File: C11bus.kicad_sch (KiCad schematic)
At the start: 44 parts, among them IC2 THVD1450DRBR, IC4 THVD1450DRBR, IC5 THVD1450DRBR, J21 Conn_01x16, J22 RTBUS.out, J23 RTBUS.in, U3 74AHC1G02, U4 74AHC1G02, U7 INA181A4

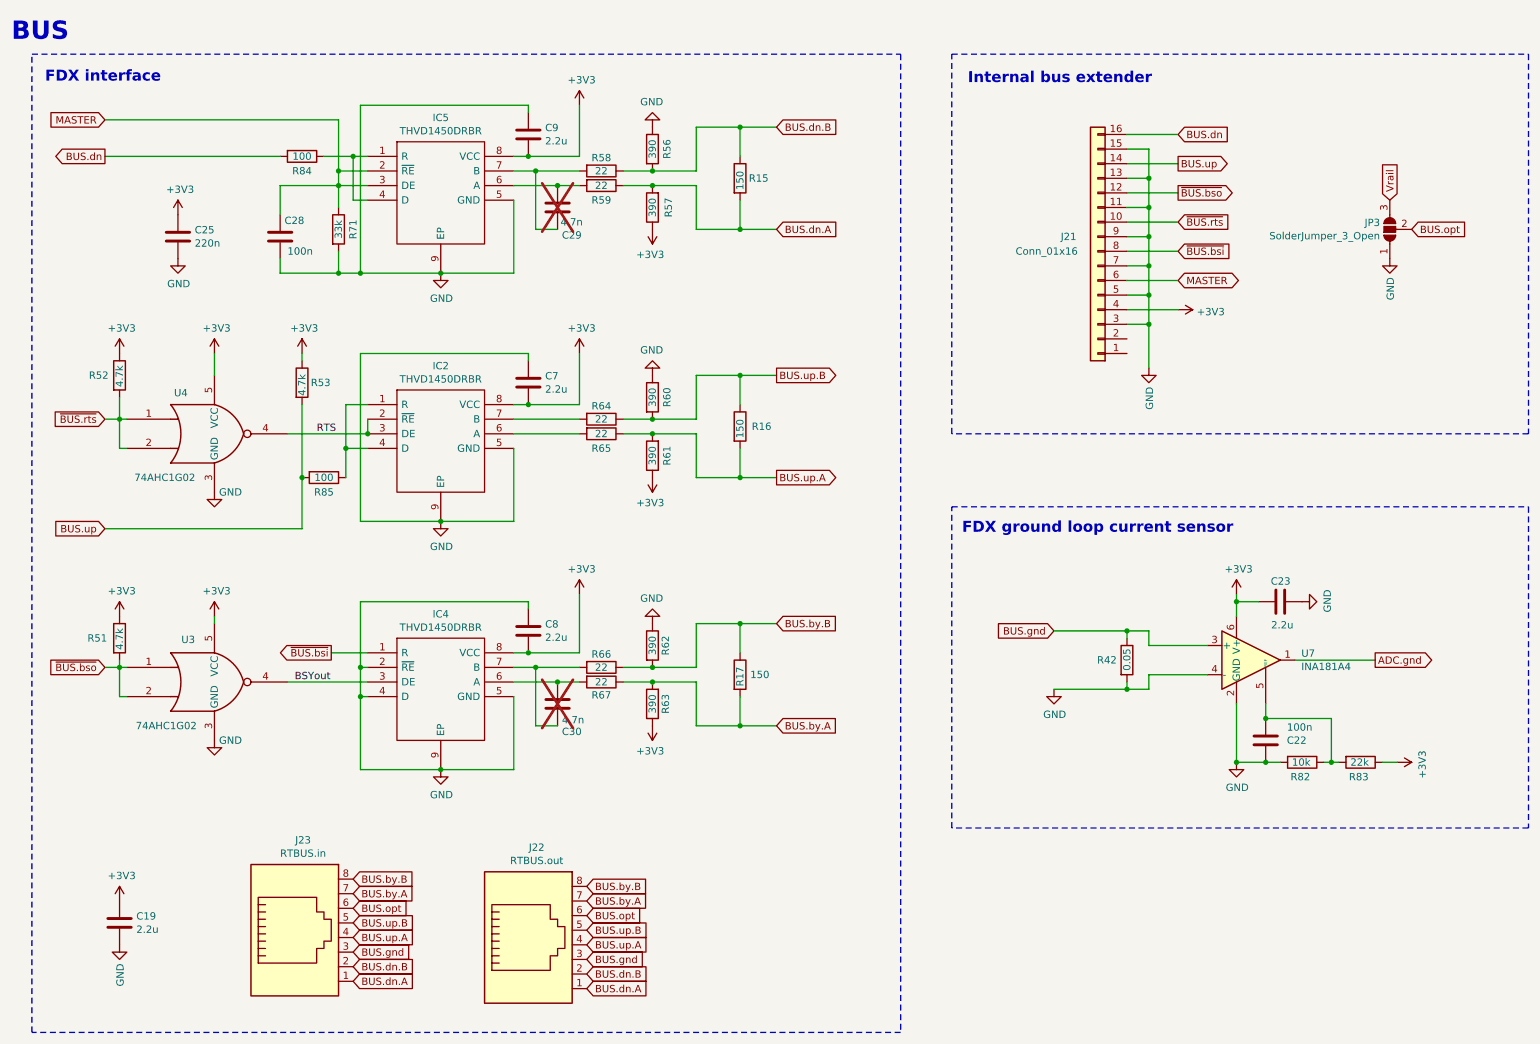
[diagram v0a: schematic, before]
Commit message: mod: changed to buck converter
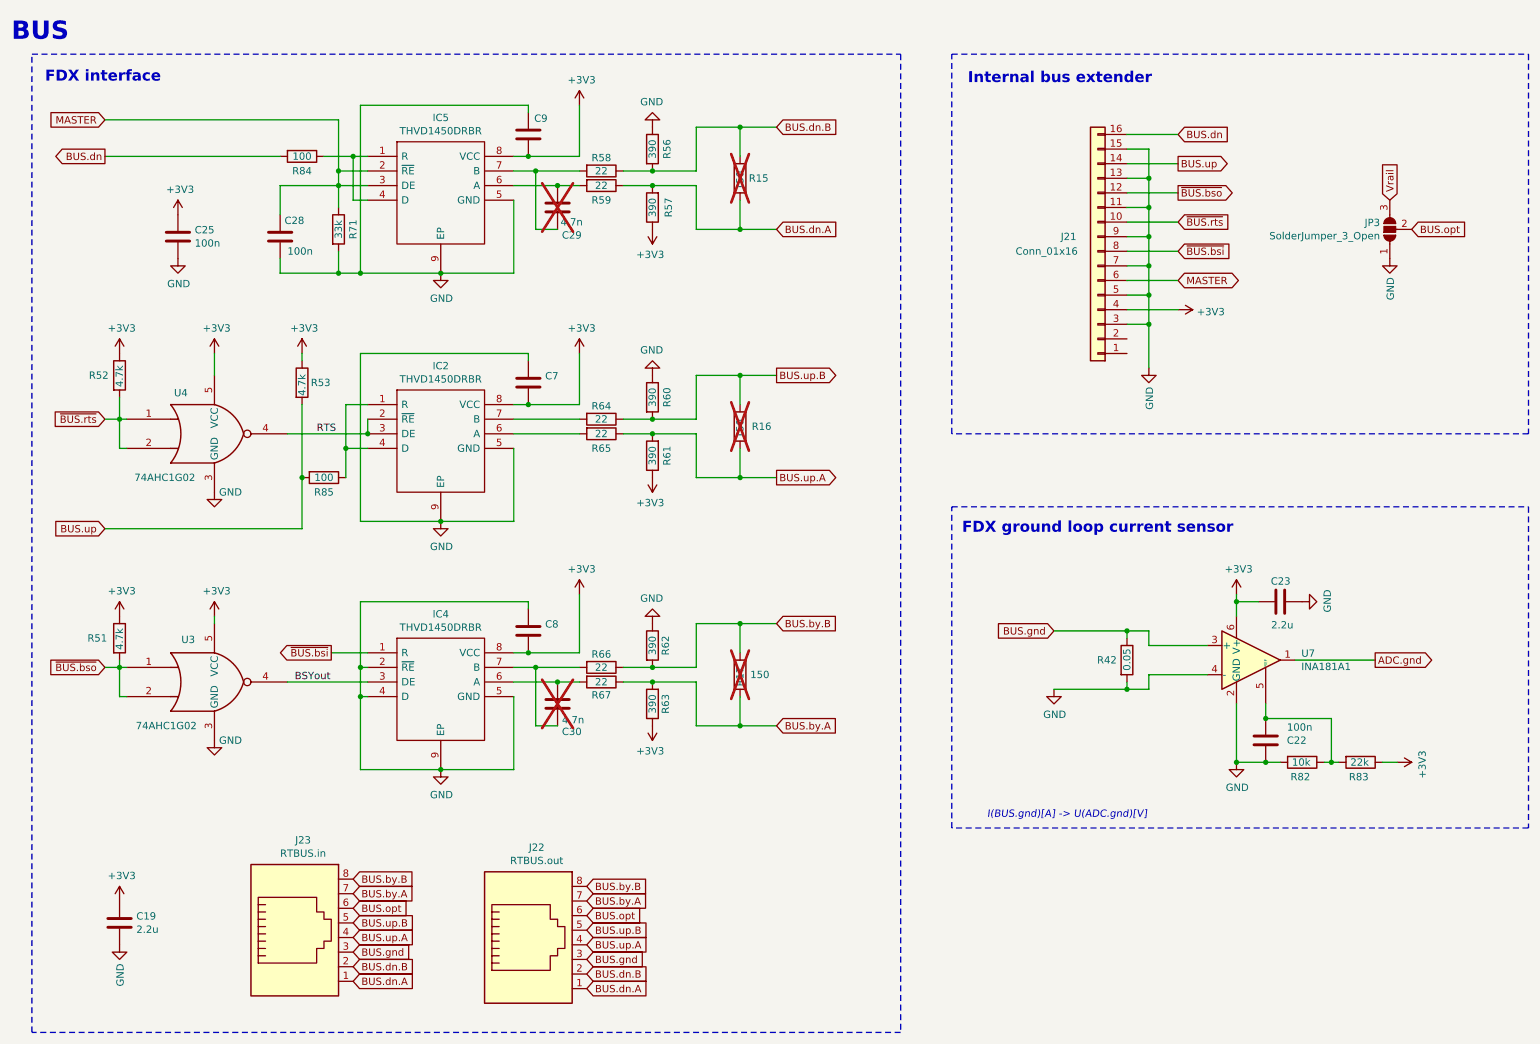
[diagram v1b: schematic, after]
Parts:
- C19: LCSC Part # (none) -> C50254
- C22, C28: LCSC Part # (none) -> C14663
- C23: footprint Capacitor_SMD:C_1206_3216Metric -> Capacitor_SMD:C_0603_1608Metric; LCSC Part # (none) -> C50254
- C25: value 220n -> 100n; LCSC Part # (none) -> C14663
- C7, C8, C9: value 2.2u -> 2.2u/50V; LCSC Part # (none) -> C50254
- IC2, IC4, IC5: Height 1 -> (none); LCSC Part # (none) -> C1850226; Manufacturer_Name Texas Instruments -> (none); Manufacturer_Part_Number THVD1450DRBR -> (none); Mouser Part Number 595-THVD1450DRBR -> (none); Mouser Price/Stock https://www.mouser.co.uk/ProductDetail/Texas-Instruments/TH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 -> (none)
- J21, J22, J23, JP3: now left out of the parts list
- R15, R16, R17: now not fitted; now left out of the parts list
- R42: LCSC Part # (none) -> C912938
- R51, R52, R53: LCSC Part # (none) -> C23162
- R56, R57, R60, R61, R62, R63: LCSC Part # (none) -> C25378
- R58, R59, R64, R65, R66, R67: LCSC Part # (none) -> C17958
- R71: LCSC Part # (none) -> C4216
- R82: LCSC Part # (none) -> C25804
- R83: LCSC Part # (none) -> C31850
- R84, R85: LCSC Part # (none) -> C25076
- U3, U4: LCSC Part # (none) -> C554271
- U7: value INA181A4 -> INA181A1; LCSC Part # (none) -> C2058943
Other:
- note added: "I(BUS.gnd)[A] -> U(ADC.gnd)[V]"

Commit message: refined BOM
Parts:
- added C33: 100n, Capacitor_SMD:C_0603_1608Metric, symbol Device:C
- added R3: 10k, Resistor_SMD:R_0603_1608Metric, symbol Device:R
- U3, U4: footprint Package_TO_SOT_SMD:SOT-353_SC-70-5 -> RTB:SOT65P210X110-5N
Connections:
- net ADC.gnd: now also C33.1, R3.1; no longer U7.1
- net GND: now also C33.2
- new net: R3.2, U7.1
